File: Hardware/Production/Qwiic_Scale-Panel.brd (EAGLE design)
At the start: 97.3 x 91.7 mm, 405 parts, among them J12 Spring Terminal, J13 Qwiic Right Angle, J14 PTH, J15 Qwiic Right Angle, J18 Spring Terminal, J19 Qwiic Right Angle, J2 Qwiic Right Angle, J20 PTH, J21 Qwiic Right Angle, J24 Spring Terminal, J25 Qwiic Right Angle, J26 PTH, J27 Qwiic Right Angle, J3 PTH, J30 Spring Terminal, J31 Qwiic Right Angle, J32 PTH, J33 Qwiic Right Angle, J36 Spring Terminal, J4 Qwiic Right Angle, J6 Qwiic Right Angle, J7 Spring Terminal, J8 PTH, J9 Qwiic Right Angle, U1 NAU7802, U2 NAU7802, U3 NAU7802, U4 NAU7802, U5 NAU7802, U6 NAU7802

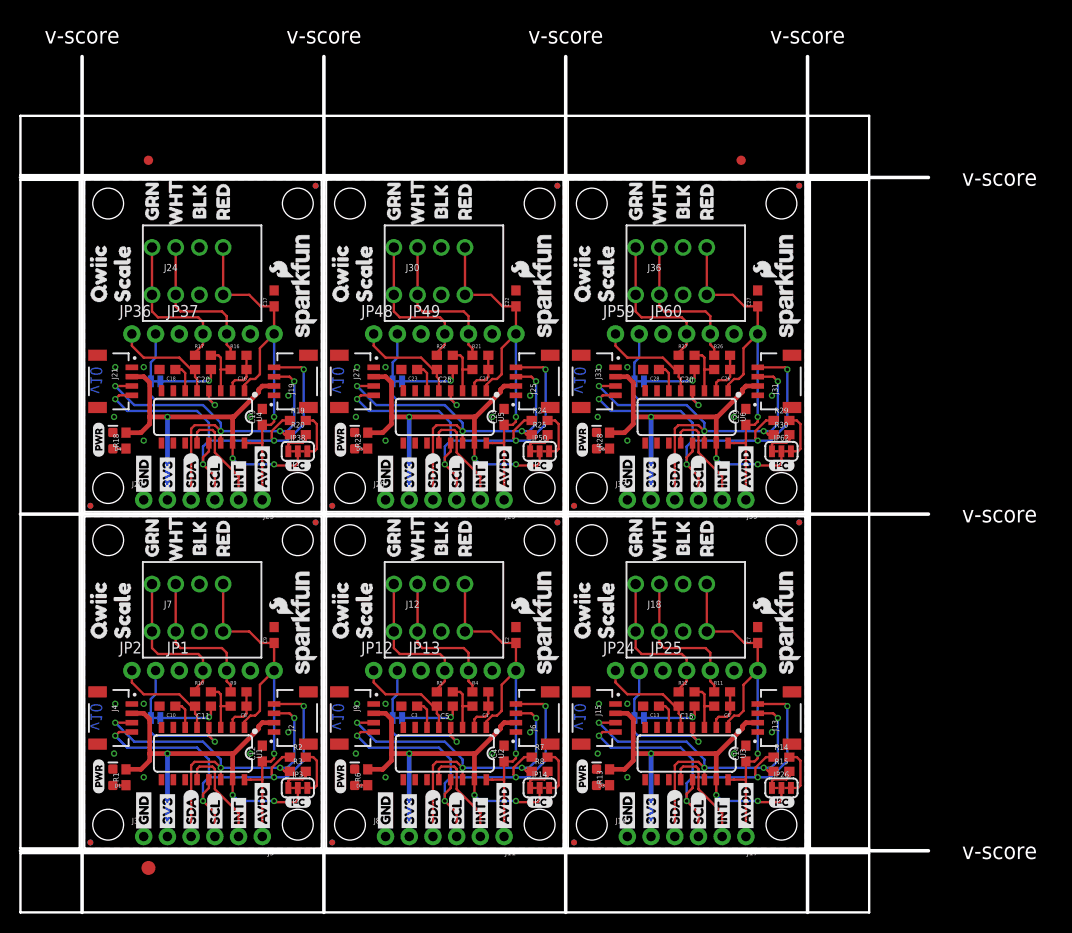
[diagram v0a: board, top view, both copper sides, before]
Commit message: Remove examples. Add proto panel. Move firmware to library repo.
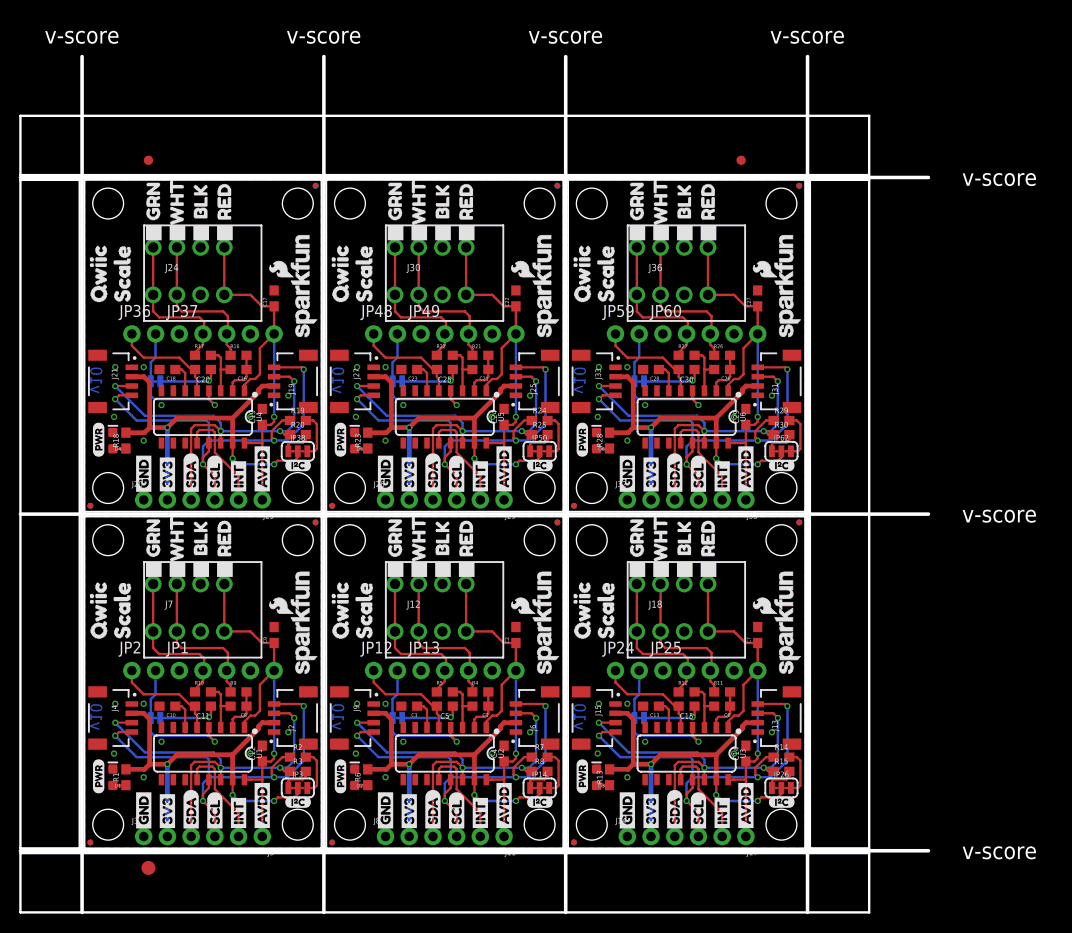
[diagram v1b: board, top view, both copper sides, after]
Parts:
- J1, J10, J16, J22, J28, J34: value (none) -> CAP
- U$104, U$139, U$174, U$209, U$69: device buzzard_labels (69):J10 -> Labels:I_SUPER2_C-()-03
- U$105, U$140, U$175, U$210, U$70: device Labels:I_SUPER2_C-()-03 -> buzzard_labels (15):CAP0
- U$14: device buzzard_labels (69):J10 -> Labels:SDA-[)
- U$20: device Labels:SDA-[) -> buzzard_labels (15):CAP0
- moved U$20 33.3 mm to (5.33, 10.9)
- moved U$14 29.9 mm to (37.3, 1.65), turned to 90 degrees
- moved U$140 17.2 mm to (5.33, 47.0), flipped to the bottom, turned to 90 degrees
- moved U$175 17.2 mm to (31.2, 47.0), flipped to the bottom, turned to 90 degrees
- moved U$70 17.2 mm to (31.2, 10.9), flipped to the bottom, turned to 90 degrees
- moved U$105 17.2 mm to (57.1, 10.9), flipped to the bottom, turned to 90 degrees
- moved U$210 17.2 mm to (57.1, 47.0), flipped to the bottom, turned to 90 degrees
- moved U$139 14.1 mm to (21.5, 41.0), flipped to the top
- moved U$174 14.1 mm to (47.4, 41.0), flipped to the top
- moved U$69 14.1 mm to (47.4, 4.95), flipped to the top
- moved U$104 14.1 mm to (73.3, 4.95), flipped to the top
- moved U$209 14.1 mm to (73.3, 41.0), flipped to the top
- moved U$122 3.30 mm to (7.37, 64.5)
- moved U$157 3.30 mm to (33.3, 64.5)
- moved U$192 3.30 mm to (59.2, 64.5)
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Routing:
- net 3.3V4: track 46.4 -> 45.3 mm
- net 3.3V3: track 46.4 -> 45.3 mm
- net 3.3V2: track 46.4 -> 45.3 mm
- net 3.3V1: track 46.4 -> 45.3 mm
- net 3.3V: track 46.4 -> 45.3 mm
- net 3.3V5: track 46.4 -> 45.3 mm
